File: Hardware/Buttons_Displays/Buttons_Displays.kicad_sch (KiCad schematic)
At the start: 10 parts, among them J1 Conn_01x10, J2 Conn_01x10, J3 Conn_01x10, J4 Conn_01x10, J5 Conn_01x10, J6 Conn_01x10, J7 Conn_01x10, J8 Conn_01x10, J9 Conn_01x03, U1 STM32H523RETx

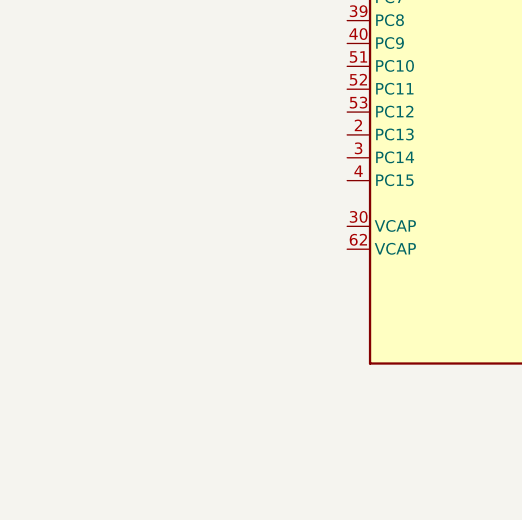
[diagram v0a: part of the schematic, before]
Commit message: Update Buttons_Displays.kicad_sch
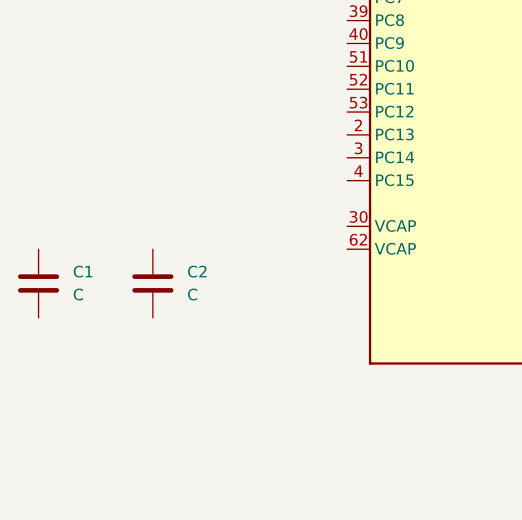
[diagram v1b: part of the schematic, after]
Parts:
- added C1, C2: C, Capacitor_SMD:C_1206_3216Metric_Pad1.33x1.80mm_HandSolder, symbol Device:C

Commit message: mierenneukerij
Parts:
- removed J2, J4, J6, J8: Conn_01x10, symbol Connector_Generic:Conn_01x10
- added C3, C4, C5, C6: 100n, Capacitor_SMD:C_1206_3216Metric_Pad1.33x1.80mm_HandSolder, symbol Device:C
- added J10, J2, J4, J6: Conn_01x08, symbol Connector_Generic:Conn_01x08
- added J11, J12, J13, J14: Conn_01x02, symbol Connector_Generic:Conn_01x02
- added R1: 10k, symbol Device:R
- added SW1: SW_SPDT, symbol Switch:SW_SPDT
- C1: value C -> 10u
- C2: value C -> 100n
- J1: footprint (none) -> ConnectorPT:1778609
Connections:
- net +3.3V: now also C1.1, C2.1, U1.1 (VBAT), U1.19 (VDD), U1.32 (VDD), U1.48 (VDD), U1.64 (VDD), C3.1, C4.1, C5.1, J10.7 (Pin_7), J2.7 (Pin_7), J4.7 (Pin_7), J6.7 (Pin_7), SW1.3 (C)
- net CS/SS: now also J10.2 (Pin_2), J2.2 (Pin_2), J4.2 (Pin_2), J6.2 (Pin_2)
- net DC1: now also J10.3 (Pin_3)
- net DC2: now also J2.3 (Pin_3)
- net DC3: now also J4.3 (Pin_3)
- net DC4: now also J6.3 (Pin_3)
- net GND: now also C1.2, C2.2, C3.2, C4.2, C5.2, C6.2, J10.8 (Pin_8), J11.1 (Pin_1), J12.1 (Pin_1), J13.1 (Pin_1), J14.1 (Pin_1), J2.8 (Pin_8), J4.8 (Pin_8), J6.8 (Pin_8), SW1.1 (A)
- net GPIO1: now also J10.1 (Pin_1)
- net GPIO2: now also J11.2 (Pin_2)
- net GPIO3: now also J2.1 (Pin_1)
- net GPIO4: now also J12.2 (Pin_2)
- net GPIO5: now also J4.1 (Pin_1)
- net GPIO6: now also J13.2 (Pin_2)
- net GPIO7: now also J6.1 (Pin_1)
- net GPIO8: now also J14.2 (Pin_2)
- net NRST: now also C6.1
- net RES1: now also J10.4 (Pin_4)
- net RES2: now also J2.4 (Pin_4)
- net RES3: now also J4.4 (Pin_4)
- net RES4: now also J6.4 (Pin_4)
- net SCLK: now also J10.6 (Pin_6), J2.6 (Pin_6), J4.6 (Pin_6), J6.6 (Pin_6)
- net at U1.60 (BOOT0): now also R1.2
- new net SW_BOOT0: R1.1, SW1.2 (B)
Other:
- moved on the sheet: C1, C2, J9

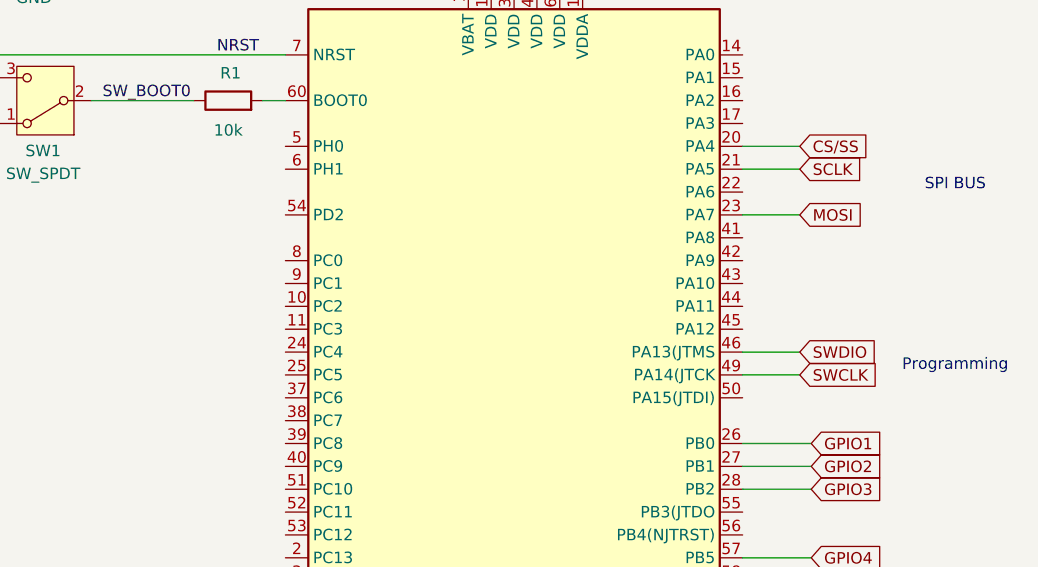
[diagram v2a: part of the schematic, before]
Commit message: Update Buttons_Displays.kicad_sch
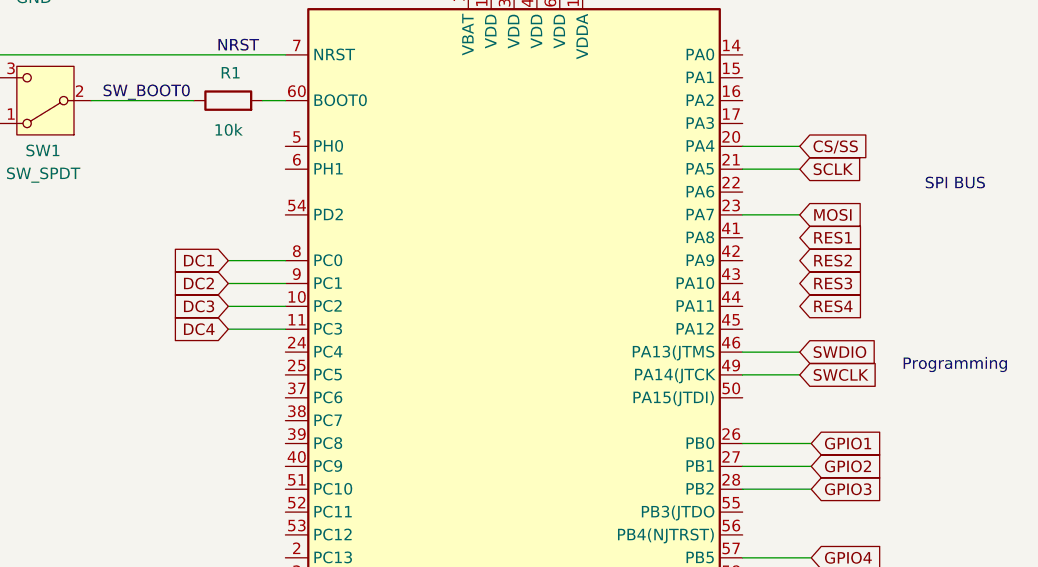
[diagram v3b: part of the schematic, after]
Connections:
- net DC1: now also U1.8 (PC0)
- net DC2: now also U1.9 (PC1)
- net DC3: now also U1.10 (PC2)
- net DC4: now also U1.11 (PC3)

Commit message: footprints
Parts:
- removed J3, J5, J7: Conn_01x10, symbol Connector_Generic:Conn_01x10
- removed R1: 10k, symbol Device:R
- added J8: i2c, Connector_pt_phoenix:1814948, symbol Connector_pt_phoenix:1814948
- added R2, R3: 4k7, Resistor_SMD:R_1206_3216Metric_Pad1.30x1.75mm_HandSolder, symbol Device:R
- added R4: 10k, Resistor_SMD:R_1206_3216Metric_Pad1.30x1.75mm_HandSolder, symbol Device:R
- J1: footprint ConnectorPT:1778609 -> (none)
- J10, J2, J4, J6: footprint (none) -> ConnectorPT:1778612
- J11, J12, J13, J14: footprint (none) -> Connector_PinSocket_2.00mm:PinSocket_1x02_P2.00mm_Vertical
- J9: footprint (none) -> Connector_PinHeader_2.54mm:PinHeader_1x03_P2.54mm_Vertical
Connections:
- net +3.3V: now also J8.2, R2.2, R3.2
- net GND: now also J10.1 (Pin_1), J2.1 (Pin_1), J4.1 (Pin_1), J6.1 (Pin_1), U1.12 (VSSA), U1.18 (VSS), U1.31 (VSS), U1.47 (VSS), U1.63 (VSS), J8.1; no longer J10.8 (Pin_8), J2.8 (Pin_8), J4.8 (Pin_8), J6.8 (Pin_8)
- net GPIO1: now also J10.8 (Pin_8); no longer J10.1 (Pin_1)
- net GPIO3: now also J2.8 (Pin_8); no longer J2.1 (Pin_1)
- net GPIO5: now also J4.8 (Pin_8); no longer J4.1 (Pin_1)
- net GPIO7: now also J6.8 (Pin_8); no longer J6.1 (Pin_1)
- net RES1: now also U1.41 (PA8)
- net RES2: now also U1.42 (PA9)
- net RES3: now also U1.43 (PA10)
- net RES4: now also U1.44 (PA11)
- net SW_BOOT0: now also R4.1
- net at U1.60 (BOOT0): now also R4.2
- net I2C1 renamed scl
- net scl: now also J8.4, R2.1; no longer U1.58 (PB6)
- new net +5Vin: J8.5
- new net sda: J8.3, R3.1, U1.58 (PB6)
